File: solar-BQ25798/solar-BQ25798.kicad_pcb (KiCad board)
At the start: 4 copper layers, 177 x 85 mm, 354 parts, among them J101 Power OUT, J102 Power In, J103 Power OUT, J1901 TC2030, Q1001 DMP2035U-7, Q1002 Q_PMOS_GSD, Q1003 FS8205A_C908265, Q101 DMP4013LFGQ-13, Q102 2N7002, Q1101 DMP2035U-7, Q1102 Q_PMOS_GSD, Q1103 FS8205A_C908265, Q1201 DMP2035U-7, Q1202 Q_PMOS_GSD, Q1203 FS8205A_C908265, Q1301 DMP2035U-7, Q1302 Q_PMOS_GSD, Q1303 FS8205A_C908265, Q1401 DMP2035U-7, Q1402 Q_PMOS_GSD, Q1403 FS8205A_C908265, Q1501 DMP2035U-7, Q1502 Q_PMOS_GSD, Q1503 FS8205A_C908265, Q1601 DMP2035U-7, Q1602 Q_PMOS_GSD, Q1603 FS8205A_C908265, Q1801 Q_PMOS_GSD, Q1802 CSD17578Q3A, Q1803 CSD17578Q3A, Q1901 2N7002, Q201 DMP2035U-7, Q202 Q_PMOS_GSD, Q203 FS8205A_C908265, Q301 DMP2035U-7, Q302 Q_PMOS_GSD, Q303 FS8205A_C908265, Q401 DMP2035U-7, Q402 Q_PMOS_GSD, Q403 FS8205A_C908265, Q501 DMP2035U-7, Q502 Q_PMOS_GSD, Q503 FS8205A_C908265, Q601 DMP2035U-7, Q602 Q_PMOS_GSD, Q603 FS8205A_C908265, Q701 DMP2035U-7, Q702 Q_PMOS_GSD, Q703 FS8205A_C908265, Q801 DMP2035U-7, Q802 Q_PMOS_GSD, Q803 FS8205A_C908265, Q901 DMP2035U-7, Q902 Q_PMOS_GSD, Q903 FS8205A_C908265, U1001 BQ297xy, U101 HT75xx-1-SOT89, U1101 BQ297xy, U1201 BQ297xy, U1301 BQ297xy, U1401 BQ297xy, U1501 BQ297xy, U1601 BQ297xy, U1701 BQ25798RQMR, U1801 BQ76920PW, U1901 ATtiny1616-M, U1902 AHT20_C2757850, U201 BQ297xy, U301 BQ297xy, U401 BQ297xy, U501 BQ297xy, U601 BQ297xy, U701 BQ297xy, U801 BQ297xy, U901 BQ297xy

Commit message: Update battery PCB
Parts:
- removed D1701: LED, LED_SMD:LED_0603_1608Metric
- removed the H109 at (72.4, -39.9)
- removed the H113 at (72.4, 39.9)
- removed JP101: Jumper_2_Open, Connector_PinHeader_2.00mm:PinHeader_2x01_P2.00mm_Vertical
- removed JP102: SolderJumper_2_Bridged, cacophony-library:SolderJumper-2_P1.3mm_Bridged_RoundedPad1.0x1.5mm
- removed the R1704 at (64.5, -0.60)
- removed the R1707 at (63.5, -7.59)
- added C103: 100n, Capacitor_SMD:C_0402_1005Metric, F.Cu at (70.8, 0.14)
- added R107: 0Ω, cacophony-library:R_1206_Shunt, F.Cu at (68.0, 3.08)
- added TP1702: TestPoint, cacophony-library:TP_PAD, B.Cu at (74.8, -10.2)
- added TP1908: TestPoint, cacophony-library:TP_PAD, B.Cu at (75.8, 10.6)
- added U102: INA219AxDCN, Package_TO_SOT_SMD:SOT-23-8, F.Cu at (68.7, -0.10)
- BAT_N101, BAT_N108, BAT_N115: footprint cacophony-library:BAT-TH_MY-18650-05-J-2 -> cacophony-library:BAT-TH-18650-N
- BAT_N102: renamed from BAT_N106; footprint cacophony-library:BAT-TH_MY-18650-05-J-2 -> cacophony-library:BAT-TH-18650-N
- BAT_N103: renamed from BAT_N111; footprint cacophony-library:BAT-TH_MY-18650-05-J-2 -> cacophony-library:BAT-TH-18650-N
- BAT_N104: renamed from BAT_N102; footprint cacophony-library:BAT-TH_MY-18650-05-J-2 -> cacophony-library:BAT-TH-18650-N
- BAT_N105: renamed from BAT_N107; footprint cacophony-library:BAT-TH_MY-18650-05-J-2 -> cacophony-library:BAT-TH-18650-N
- BAT_N106: renamed from BAT_N112; footprint cacophony-library:BAT-TH_MY-18650-05-J-2 -> cacophony-library:BAT-TH-18650-N
- BAT_N107: renamed from BAT_N103; footprint cacophony-library:BAT-TH_MY-18650-05-J-2 -> cacophony-library:BAT-TH-18650-N
- BAT_N109: renamed from BAT_N113; footprint cacophony-library:BAT-TH_MY-18650-05-J-2 -> cacophony-library:BAT-TH-18650-N
- BAT_N110: renamed from BAT_N104; footprint cacophony-library:BAT-TH_MY-18650-05-J-2 -> cacophony-library:BAT-TH-18650-N
- BAT_N111: renamed from BAT_N109; footprint cacophony-library:BAT-TH_MY-18650-05-J-2 -> cacophony-library:BAT-TH-18650-N
- BAT_N112: renamed from BAT_N114; footprint cacophony-library:BAT-TH_MY-18650-05-J-2 -> cacophony-library:BAT-TH-18650-N
- BAT_N113: renamed from BAT_N105; footprint cacophony-library:BAT-TH_MY-18650-05-J-2 -> cacophony-library:BAT-TH-18650-N
- BAT_N114: renamed from BAT_N110; footprint cacophony-library:BAT-TH_MY-18650-05-J-2 -> cacophony-library:BAT-TH-18650-N
- BAT_P101, BAT_P108, BAT_P115: footprint cacophony-library:BAT-TH_MY-18650-test8_4.0_2.5 -> cacophony-library:BAT-TH-18650-P_silkscreen
- BAT_P102: renamed from BAT_P106; footprint cacophony-library:BAT-TH_MY-18650-test8_4.0_2.5 -> cacophony-library:BAT-TH-18650-P_silkscreen
- BAT_P103: renamed from BAT_P111; footprint cacophony-library:BAT-TH_MY-18650-test8_4.0_2.5 -> cacophony-library:BAT-TH-18650-P_silkscreen
- BAT_P104: renamed from BAT_P102; footprint cacophony-library:BAT-TH_MY-18650-test8_4.0_2.5 -> cacophony-library:BAT-TH-18650-P_silkscreen
- BAT_P105: renamed from BAT_P107; footprint cacophony-library:BAT-TH_MY-18650-test8_4.0_2.5 -> cacophony-library:BAT-TH-18650-P_silkscreen
- BAT_P106: renamed from BAT_P112; footprint cacophony-library:BAT-TH_MY-18650-test8_4.0_2.5 -> cacophony-library:BAT-TH-18650-P_silkscreen
- BAT_P107: renamed from BAT_P103; footprint cacophony-library:BAT-TH_MY-18650-test8_4.0_2.5 -> cacophony-library:BAT-TH-18650-P_silkscreen
- BAT_P109: renamed from BAT_P113; footprint cacophony-library:BAT-TH_MY-18650-test8_4.0_2.5 -> cacophony-library:BAT-TH-18650-P_silkscreen
- BAT_P110: renamed from BAT_P104; footprint cacophony-library:BAT-TH_MY-18650-test8_4.0_2.5 -> cacophony-library:BAT-TH-18650-P_silkscreen
- BAT_P111: renamed from BAT_P109; footprint cacophony-library:BAT-TH_MY-18650-test8_4.0_2.5 -> cacophony-library:BAT-TH-18650-P_silkscreen
- BAT_P112: renamed from BAT_P114; footprint cacophony-library:BAT-TH_MY-18650-test8_4.0_2.5 -> cacophony-library:BAT-TH-18650-P_silkscreen
- BAT_P113: renamed from BAT_P105; footprint cacophony-library:BAT-TH_MY-18650-test8_4.0_2.5 -> cacophony-library:BAT-TH-18650-P_silkscreen
- BAT_P114: renamed from BAT_P110; footprint cacophony-library:BAT-TH_MY-18650-test8_4.0_2.5 -> cacophony-library:BAT-TH-18650-P_silkscreen
- C1701: renamed from C1709; moved to B.Cu
- C1706: renamed from C1718; footprint Capacitor_SMD:C_0603_1608Metric -> Capacitor_SMD:C_0402_1005Metric; moved to B.Cu
- C1707: renamed from C1721; footprint Capacitor_SMD:C_0603_1608Metric -> Capacitor_SMD:C_0402_1005Metric; moved to B.Cu
- C1710: renamed from C1720; footprint Capacitor_SMD:C_0603_1608Metric -> Capacitor_SMD:C_0402_1005Metric
- C1711, D1901, Q1901, R1708: moved to B.Cu
- C1712: renamed from C1722; moved to B.Cu
- C1713: renamed from C1712; moved to B.Cu
- C1720: renamed from C1702; moved to B.Cu
- C1722: renamed from C1703; moved to B.Cu
- L1701: footprint Inductor_SMD:L_TDK_SLF10165 -> Inductor_SMD:L_12x12mm_H8mm
- R103: value 30k -> 100k
- R104: value 10k -> 100k
- R1701: renamed from R1703; moved to B.Cu
- R1703: renamed from R1701; moved to B.Cu
- R1705: renamed from R1702; moved to B.Cu
- R1707: renamed from R1706; moved to B.Cu
- R1902: renamed from R1904; moved to B.Cu
- moved R1701 24.4 mm to (72.6, -11.7), turned to 0 degrees
- moved C1701 20.6 mm to (72.6, -13.6), turned to 180 degrees
- moved R103 19.7 mm to (67.7, -3.08)
- moved Q1901 19.6 mm to (75.1, -29.6), turned to 180 degrees
- moved R1902 18.5 mm to (75.9, -32.3), turned to 180 degrees
- moved R104 18.1 mm to (68.6, -3.08)
- moved R101 17.2 mm to (71.8, -15.9), turned to 90 degrees
- moved D103 15.6 mm to (71.8, -19.2), turned to -90 degrees
- moved D1901 14.9 mm to (78.8, -30.9)
- moved FL101 12.2 mm to (80.1, -21.2), turned to -90 degrees
- moved BUZZER1901 11.4 mm to (71.4, -30.1)
- moved C1702 10.4 mm to (75.6, -20.1), turned to 90 degrees
- moved Q101 10.2 mm to (74.9, -17.1), turned to 90 degrees
- moved C1703 9.78 mm to (72.6, -11.5)
- moved C1704 9.78 mm to (72.6, -13.8)
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- renumbered BUZZER1902 to BUZZER1901, C1708 to C1702, C1705 to C1703, C1706 to C1704, C1707 to C1705, C1710 to C1708, C1723 to C1709, C1716 to C1714, C1713 to C1715, C1717 to C1716, C1701 to C1717, C1714 to C1718, C1715 to C1721, C1704 to C1723, C1810 to C1801, C1811 to C1802, C1801 to C1803, C1803 to C1804, C1804 to C1805, C1805 to C1806, C1808 to C1807, C1812 to C1808, C1813 to C1809, C1802 to C1810, C1809 to C1811, C1807 to C1812, C1806 to C1813, C1902 to C1901, C1901 to C1902, D102 to D101, D103 to D102, D101 to D103, F102 to F101, F101 to F102, FL102 to FL101, FL101 to FL102, H105 to H102, H117 to H105, H121 to H106, H125 to H107, H129 to H108, H102 to H109, H106 to H110, H110 to H111, H114 to H112, H118 to H113, H122 to H114, H126 to H115, H130 to H116, H103 to H117, H107 to H118, H111 to H119, H115 to H120, H119 to H121, H123 to H122, H127 to H123, H131 to H124, H104 to H125, H108 to H126, H112 to H127, H116 to H128, H120 to H129, H124 to H130, H128 to H131, J102 to J101, J101 to J102, Q1802 to Q1801, Q1801 to Q1802, R1003 to R1002, R1002 to R1003, R1007 to R1004, R1004 to R1005, R1005 to R1006, R1006 to R1007, R102 to R101, R101 to R102, R1103 to R1102, R1102 to R1103, R1107 to R1104, R1104 to R1105, R1105 to R1106, R1106 to R1107, R1203 to R1202, R1202 to R1203, R1207 to R1204, R1204 to R1205, R1205 to R1206, R1206 to R1207, R1303 to R1302, R1302 to R1303, R1307 to R1304, R1304 to R1305, R1305 to R1306, R1306 to R1307, R1403 to R1402, R1402 to R1403, R1407 to R1404, R1404 to R1405, R1405 to R1406, R1406 to R1407, R1503 to R1502, R1502 to R1503, R1507 to R1504, R1504 to R1505, R1505 to R1506, R1506 to R1507, R1603 to R1602, R1602 to R1603, R1607 to R1604, R1604 to R1605, R1605 to R1606, R1606 to R1607, R1705 to R1704, R1802 to R1801, R1803 to R1802, R1804 to R1803, R1805 to R1804, R1807 to R1805, R1808 to R1806, R1810 to R1807, R1814 to R1808, R1811 to R1809, R1812 to R1810, R1801 to R1811, R1809 to R1812, R1806 to R1814, R1906 to R1901, R1905 to R1904, R1901 to R1905, R1902 to R1906, R203 to R202, R202 to R203, R207 to R204, R204 to R205, R205 to R206, R206 to R207, R303 to R302, R302 to R303, R307 to R304, R304 to R305, R305 to R306, R306 to R307, R403 to R402, R402 to R403, R407 to R404, R404 to R405, R405 to R406, R406 to R407, R503 to R502, R502 to R503, R507 to R504, R504 to R505, R505 to R506, R506 to R507, R603 to R602, R602 to R603, R607 to R604, R604 to R605, R605 to R606, R606 to R607, R703 to R702, R702 to R703, R707 to R704, R704 to R705, R705 to R706, R706 to R707, R803 to R802, R802 to R803, R807 to R804, R804 to R805, R805 to R806, R806 to R807, R903 to R902, R902 to R903, R907 to R904, R904 to R905, R905 to R906, R906 to R907, TP1903 to TP1901, TP1904 to TP1902, TP1905 to TP1903, TP1901 to TP1904, TP1902 to TP1905, U1902 to U1901, U1901 to U1902
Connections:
- net Net-(U1701-BTST1) renamed /BQ25798/BTST1
- net Net-(U1701-BTST2) renamed /BQ25798/BTST2
- net Net-(U1701-PROG) renamed /BQ25798/PROG
- FL101 pad 1: /POWER_IN_FUSED -> /GND_IN_PHY
- FL101 pad 2: /GND_IN_PHY -> /POWER_IN_FUSED
- FL101 pad 3: GND -> /POWER_IN_FILTERED
- FL101 pad 4: /POWER_IN_FILTERED -> GND
- R103 pad 1: /V_{SENSE} -> Net-(U102-A1)
- R103 pad 2: SENSE_DIV -> GND
- R104 pad 1: SENSE_DIV -> Net-(U102-A0)
- U1701 pad 1: /BQ25798/STAT_PHY -> Net-(U1701-STAT)
- U1902 pad 17: SENSE_DIV -> Net-(U1902-PC2)
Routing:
- net GND: track 87.1 -> 125.1 mm, vias 107 -> 112
- net BUZZER: track 32.5 -> 60.9 mm, vias 0 -> 3
- net +3.3V: track 49.1 -> 72.5 mm, vias 4 -> 7
- net ~{CE}: track 19.4 -> 39.5 mm
- net SENSE_DIV: track 17.9 -> 0.00 mm
- net TX: track 28.3 -> 44.7 mm, vias 2 -> 1
- net PRE_LIN_REG: track 31.2 -> 46.4 mm, vias 1 -> 0
- net /GND_IN_PHY: track 20.8 -> 7.41 mm
- net /BQ25798/SW1: track 15.1 -> 3.84 mm, vias 0 -> 10
- net PMID: track 12.0 -> 1.51 mm, vias 0 -> 4
- net REGN: track 18.7 -> 8.23 mm, vias 2 -> 1
- net PACK_+: track 69.0 -> 79.4 mm, vias 40 -> 17
- net /BQ25798/STAT_PHY: track 9.32 -> 0.00 mm, vias 2 -> 0
- net /BQ25798/BTST2: track 9.56 -> 1.44 mm, vias 2 -> 1
- net /BQ25798/TS: track 80.4 -> 87.9 mm
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- added copper zone on B.Cu, net /BQ25798/SW1
- added copper zone on B.Cu, net /BQ25798/SW2
- added copper zone on B.Cu, net PMID
- added copper zone on F.Cu, net PMID
- removed copper zone on F.Cu, net V_{IN}

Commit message: Update shunt resistor
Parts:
- R1808: value 1mΩ -> 5mΩ
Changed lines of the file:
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@@
 			)
 		)
-		(property "Value" "1mΩ"
+		(property "Value" "5mΩ"
 			(at 0 1.82 0)
 			(layer "F.Fab")
@@
 			)
 		)
-		(property "LCSC Part" "C7467246"
+		(property "LCSC Part" "C2988648"
 			(at 0 0 0)
 			(unlocked yes)

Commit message: Update case and minor PCB changes
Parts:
- moved R1904 3.91 mm to (82.6, 2.77)
- moved D1902 3.61 mm to (85.0, 2.90)
- moved Q102 3.26 mm to (84.8, 9.46)
- moved TP1906 1.75 mm to (85.1, -18.7)
- moved TP1905 1.39 mm to (80.2, 3.21)
- moved J1901 0.50 mm to (85.6, -14.9)
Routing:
- net RX: track 33.4 -> 40.3 mm
- net ~{CE}: track 39.5 -> 32.8 mm
- net /ATtiny1616/UPDI: track 31.2 -> 35.6 mm
- net /ATtiny1616/LED_PHY: track 4.84 -> 8.62 mm
- net PULL_SENSE_LOW: track 15.1 -> 11.3 mm
- net ~{INT}: track 25.8 -> 23.6 mm
- net ALERT: track 25.2 -> 26.9 mm
- net SDA: track 45.6 -> 44.0 mm
- net PRE_LIN_REG: track 46.4 -> 44.8 mm
- net Net-(U1902-PA4): track 2.17 -> 3.36 mm
- net TS1: track 60.2 -> 61.3 mm
- net /V_{SENSE}: track 18.6 -> 17.7 mm
- net SCL: track 49.5 -> 48.7 mm
- net PACK_+: track 79.4 -> 78.9 mm, vias 17 -> 34
- net GND: track 125.1 -> 125.6 mm, vias 112 -> 116

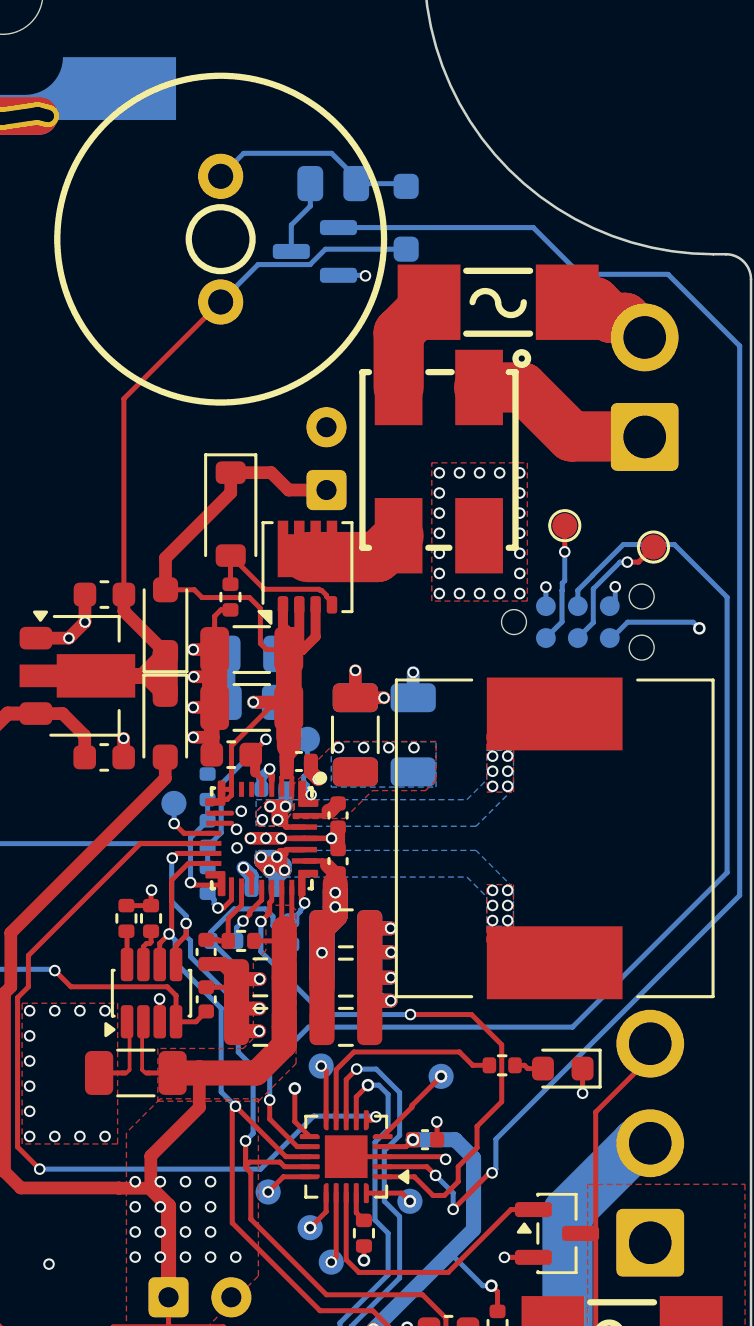
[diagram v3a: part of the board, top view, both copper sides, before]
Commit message: Fix buzzer
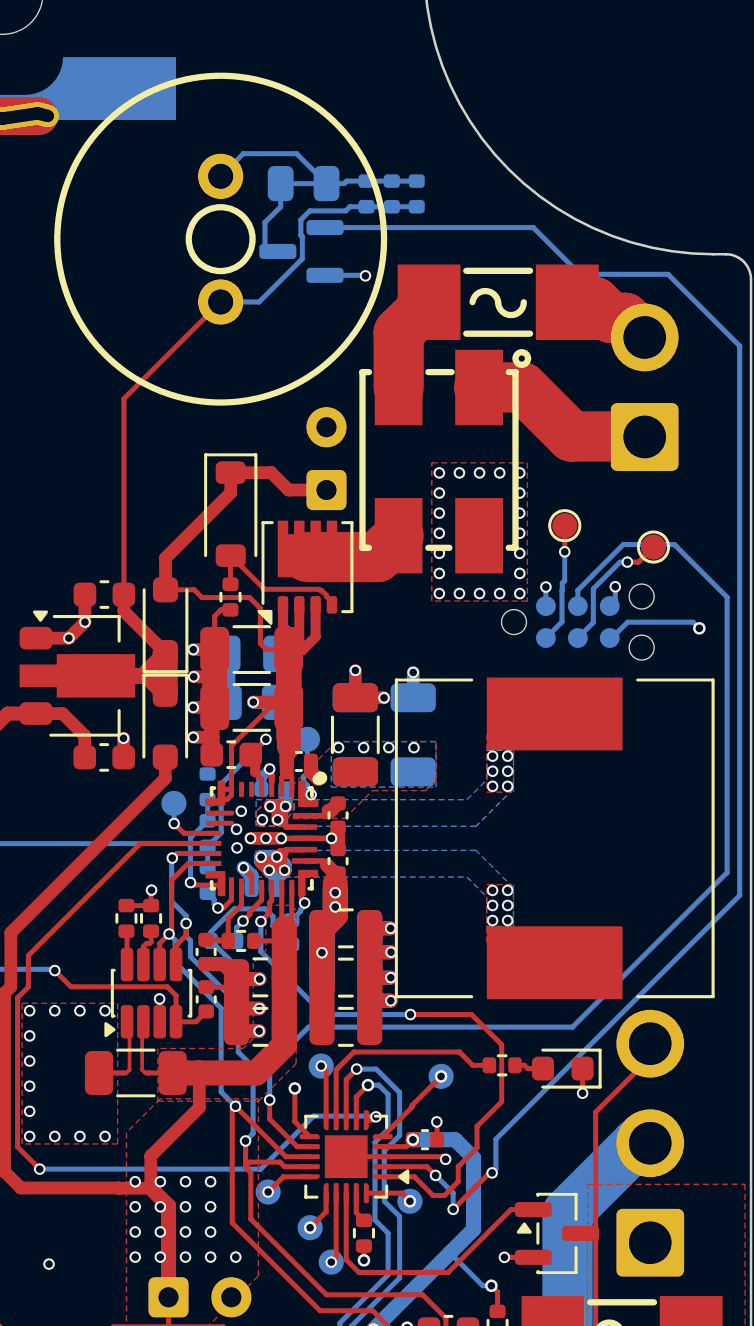
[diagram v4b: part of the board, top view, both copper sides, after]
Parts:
- removed D1901: D, Diode_SMD:D_SOD-323_HandSoldering
- added R2: 10k, Resistor_SMD:R_0402_1005Metric, B.Cu at (79.2, -31.9)
- added R3: 10k, Resistor_SMD:R_0402_1005Metric, B.Cu at (78.2, -31.9)
- added R4: 10k, Resistor_SMD:R_0402_1005Metric, B.Cu at (77.2, -31.9)
- R1902: footprint Resistor_SMD:R_0805_2012Metric -> cacophony-library:R_0805_0Ω_Short
- moved R1902 1.18 mm to (74.7, -32.3)
- moved Q1901 0.54 mm to (74.6, -29.6)
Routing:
- net PRE_LIN_REG: track 44.8 -> 47.0 mm
- net BUZZER: track 60.9 -> 62.0 mm
- net Net-(BUZZER1901-Pad2): track 8.05 -> 8.71 mm
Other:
- board text added: "${HASH}"
